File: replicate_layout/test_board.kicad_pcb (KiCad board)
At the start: 2 copper layers, 30 parts, among them J1001 Pusa_4mm, J1002 Pusa_4mm, Q1001 CSD19531KCS, Q1002 CSD19531KCS, Q1003 CSD19531KCS, Q2001 CSD19531KCS, Q2002 CSD19531KCS, Q3001 CSD19531KCS, Q3002 CSD19531KCS, Q4001 CSD19531KCS, Q4002 CSD19531KCS, U1001 LAUNCHXL-F28377S, U2001 IR2181, U3001 IR2181, U4001 IR2181

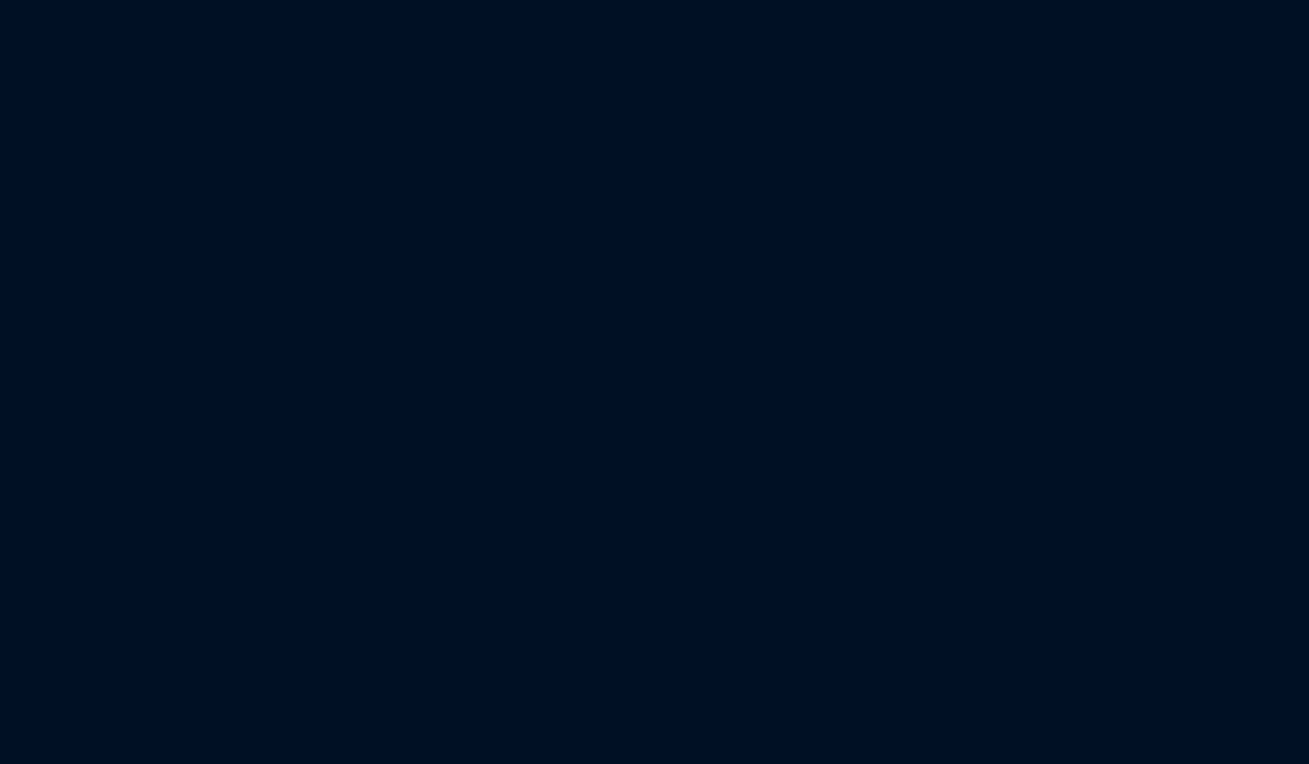
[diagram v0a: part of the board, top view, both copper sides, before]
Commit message: Pre-fill minimum replication steps. Modifed test cases
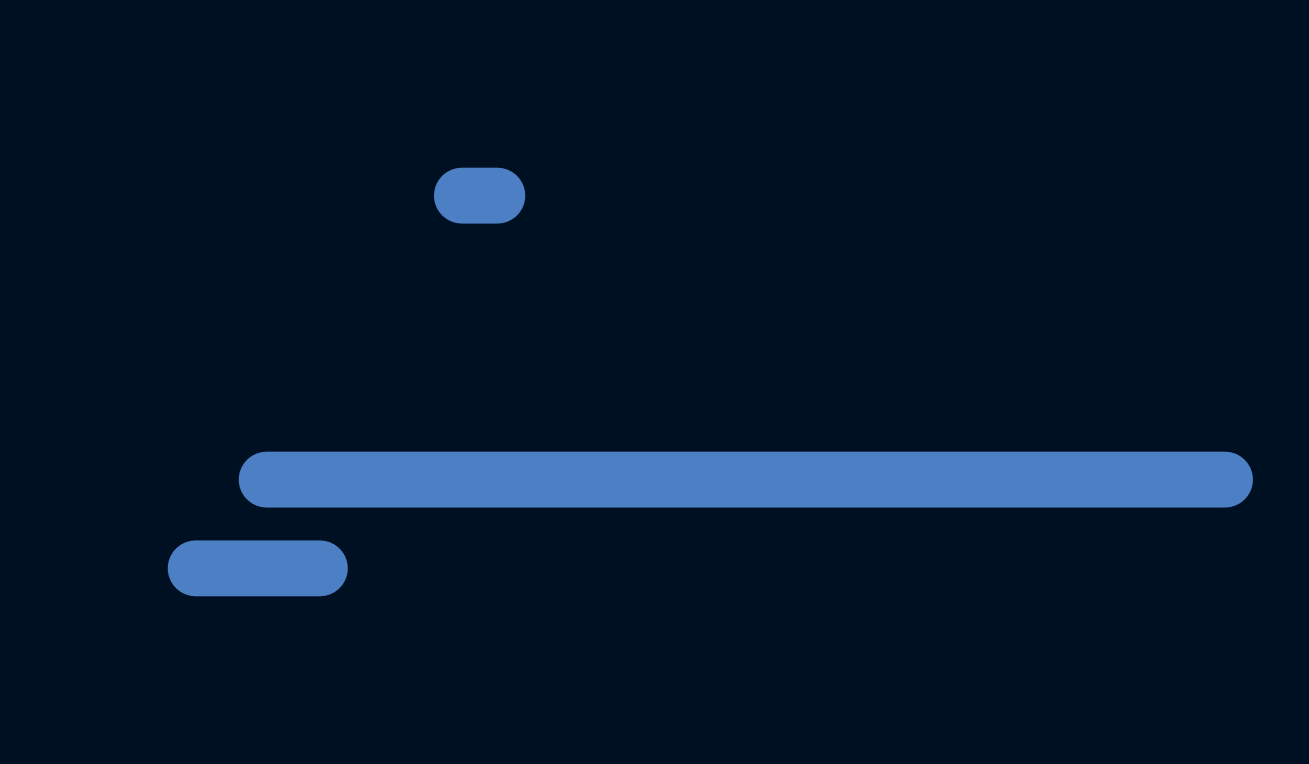
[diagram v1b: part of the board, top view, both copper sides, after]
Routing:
- net (no net): track 19.9 -> 59.9 mm

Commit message: changed test setup
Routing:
- net +VDC: track 14.5 -> 74.4 mm
- net (no net): track 59.9 -> 0.00 mm
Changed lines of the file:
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@@
   )
   (setup
-    (last_trace_width 2)
+    (last_trace_width 0.25)
     (user_trace_width 0.5)
     (user_trace_width 1)
@@
       (net 2 GND))
   )
-  (segment (start 224.79 100.33) (end 226.06 100.33) (width 2) (layer B.Cu) (net 0))
-  (segment (start 215.265 113.665) (end 219.71 113.665) (width 2) (layer B.Cu) (net 0))
-  (segment (start 217.805 110.49) (end 252.095 110.49) (width 2) (layer B.Cu) (net 0))
-  (segment (start 229.87 91.44) (end 229.87 92.075) (width 2) (layer F.Cu) (net 0))
-  (segment (start 234.95 86.36) (end 229.87 91.44) (width 2) (layer F.Cu) (net 0))
-  (segment (start 247.015 86.36) (end 234.95 86.36) (width 2) (layer F.Cu) (net 0))
+  (segment (start 224.79 100.33) (end 226.06 100.33) (width 2) (layer B.Cu) (net 5))
+  (segment (start 215.265 113.665) (end 219.71 113.665) (width 2) (layer B.Cu) (net 5))
+  (segment (start 217.805 110.49) (end 252.095 110.49) (width 2) (layer B.Cu) (net 5))
+  (segment (start 229.87 91.44) (end 229.87 92.075) (width 2) (layer F.Cu) (net 5))
+  (segment (start 234.95 86.36) (end 229.87 91.44) (width 2) (layer F.Cu) (net 5))
+  (segment (start 247.015 86.36) (end 234.95 86.36) (width 2) (layer F.Cu) (net 5))
   (segment (start 177.8 102.715) (end 177.8 106.235) (width 0.5) (layer F.Cu) (net 1))
   (segment (start 177.8 106.235) (end 178.245 106.68) (width 0.5) (layer F.Cu) (net 1))

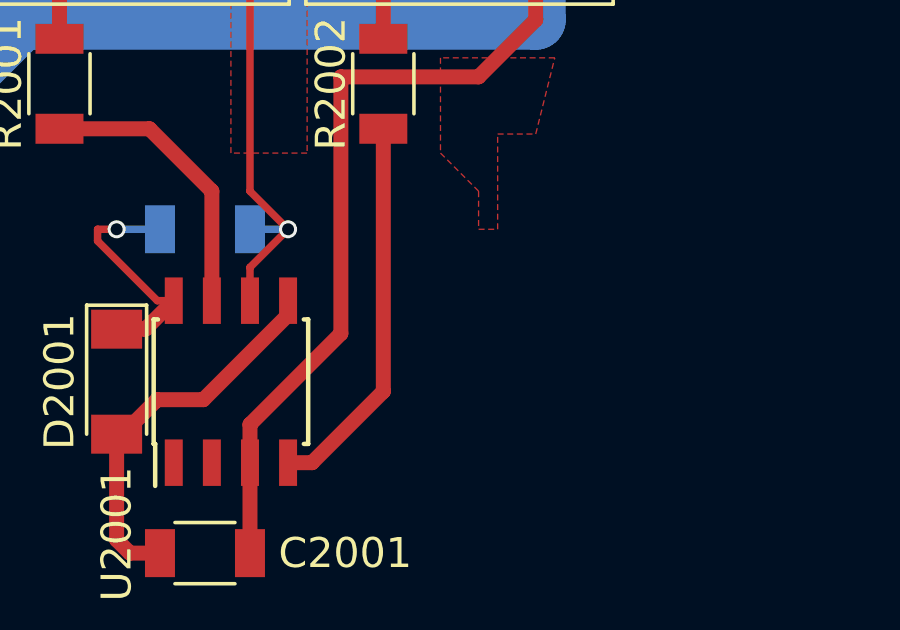
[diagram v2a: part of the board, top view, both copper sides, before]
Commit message: replicates also zones not on a copper layer (bugfix) added formbuilder file
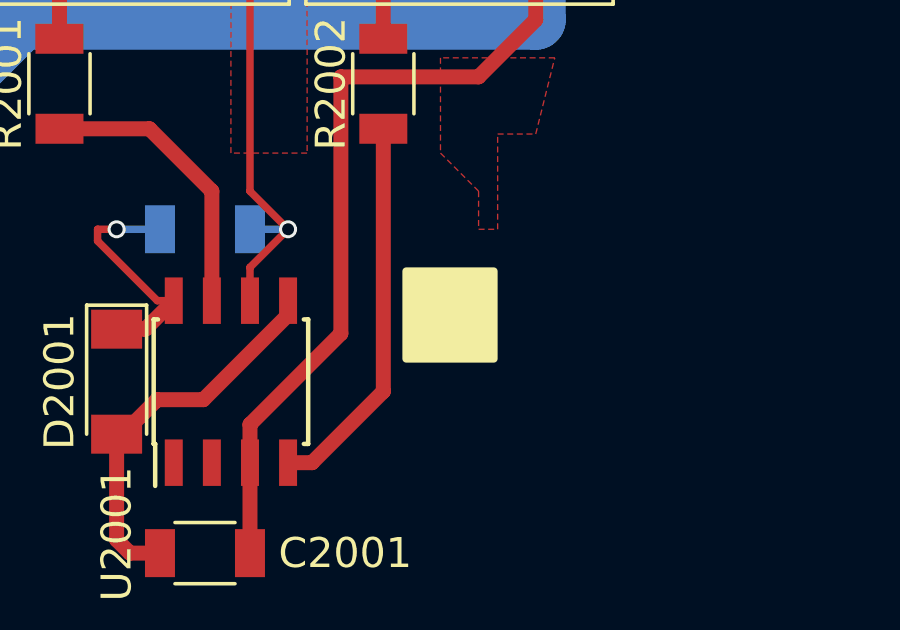
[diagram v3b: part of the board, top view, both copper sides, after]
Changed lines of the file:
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@@
+    )
+  )
+  (zone (net 0) (net_name "") (layer F.SilkS) (hatch edge 0.508)
+    (connect_pads (clearance 0.508))
+    (min_thickness 0.254)
+    (fill yes (arc_segments 16) (thermal_gap 0.508) (thermal_bridge_width 0.508))
+    (polygon
+      (pts
+        (xy 187.325 97.155) (xy 190.5 97.155) (xy 190.5 100.33) (xy 187.325 100.33)
+      )
     )
   )

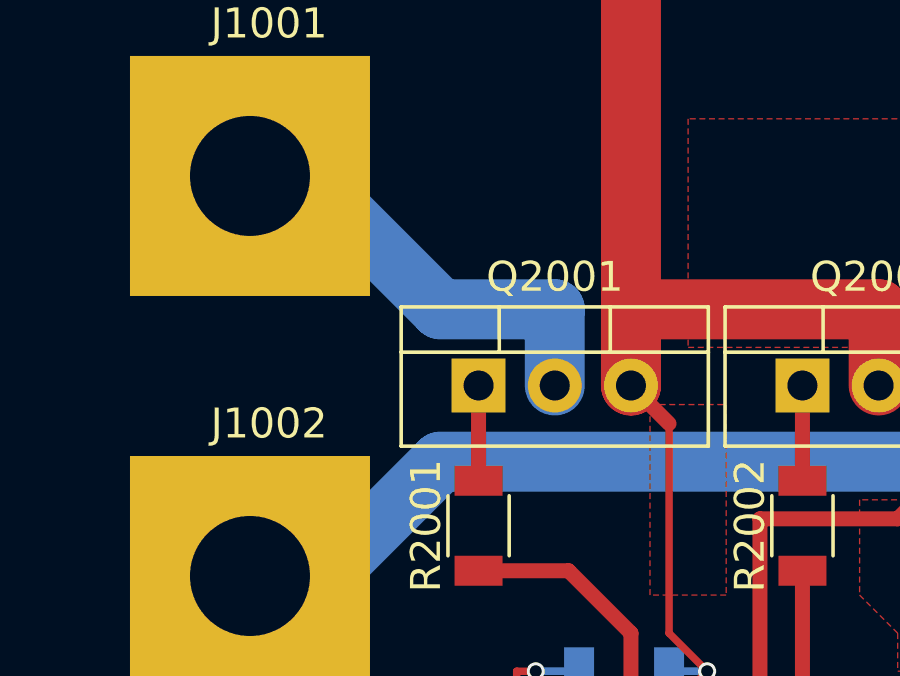
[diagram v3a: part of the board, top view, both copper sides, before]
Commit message: Added replication of tracks which are outside of bounding box but are on nets which are contained only within the sheet to be replicated.
updated test layouts.
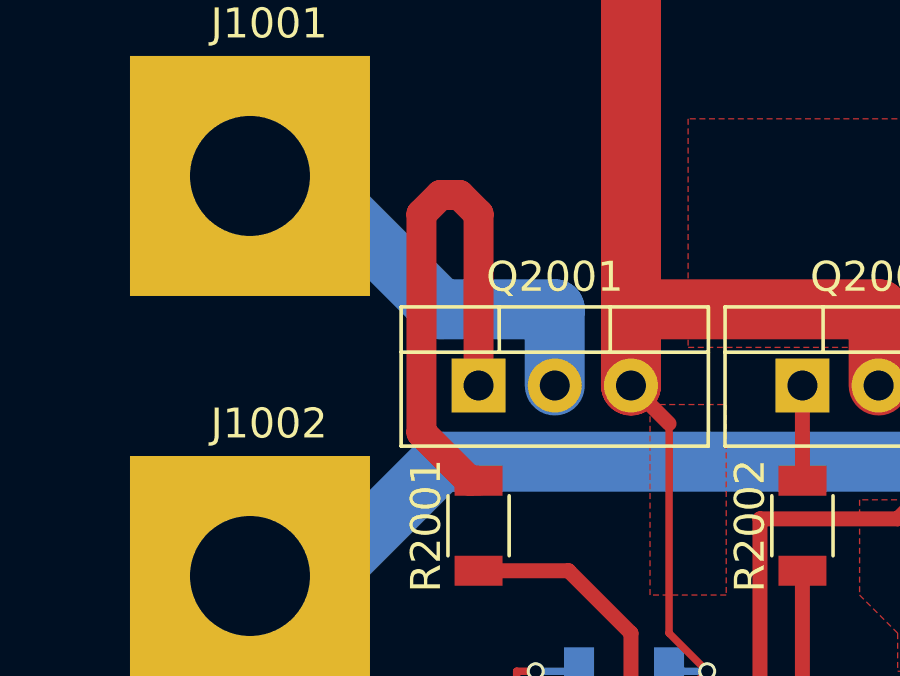
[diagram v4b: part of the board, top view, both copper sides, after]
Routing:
- net /Veja_1/QH_G: track 3.17 -> 18.0 mm
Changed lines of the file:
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@@
     (thickness 1.6)
     (drawings 0)
-    (tracks 56)
+    (tracks 62)
     (zones 0)
     (modules 30)
@@
   )
   (setup
-    (last_trace_width 0.25)
+    (last_trace_width 1)
     (user_trace_width 0.5)
     (user_trace_width 1)
@@
   (segment (start 178.895 92.535) (end 175.895 92.535) (width 0.5) (layer F.Cu) (net 14))
   (segment (start 180.975 98.265) (end 180.975 94.615) (width 0.5) (layer F.Cu) (net 14))
-  (segment (start 175.895 86.36) (end 175.895 89.535) (width 0.5) (layer F.Cu) (net 19))
+  (segment (start 175.26 80.01) (end 175.895 80.645) (width 1) (layer F.Cu) (net 19))
+  (segment (start 175.895 80.645) (end 175.895 86.36) (width 1) (layer F.Cu) (net 19))
+  (segment (start 174.625 80.01) (end 175.26 80.01) (width 1) (layer F.Cu) (net 19))
+  (segment (start 173.99 80.645) (end 174.625 80.01) (width 1) (layer F.Cu) (net 19))
+  (segment (start 173.99 87.93) (end 173.99 80.645) (width 1) (layer F.Cu) (net 19))
+  (segment (start 175.895 89.535) (end 175.595 89.535) (width 1) (layer F.Cu) (net 19))
+  (segment (start 175.595 89.535) (end 173.99 87.93) (width 1) (layer F.Cu) (net 19))
   (segment (start 186.69 86.36) (end 186.69 89.535) (width 0.5) (layer F.Cu) (net 20))
   (segment (start 186.69 92.535) (end 186.69 101.29) (width 0.5) (layer F.Cu) (net 25))
